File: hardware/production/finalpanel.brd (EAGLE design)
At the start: 166.7 x 33 mm, 49 parts, among them IC1 ATMEGA88

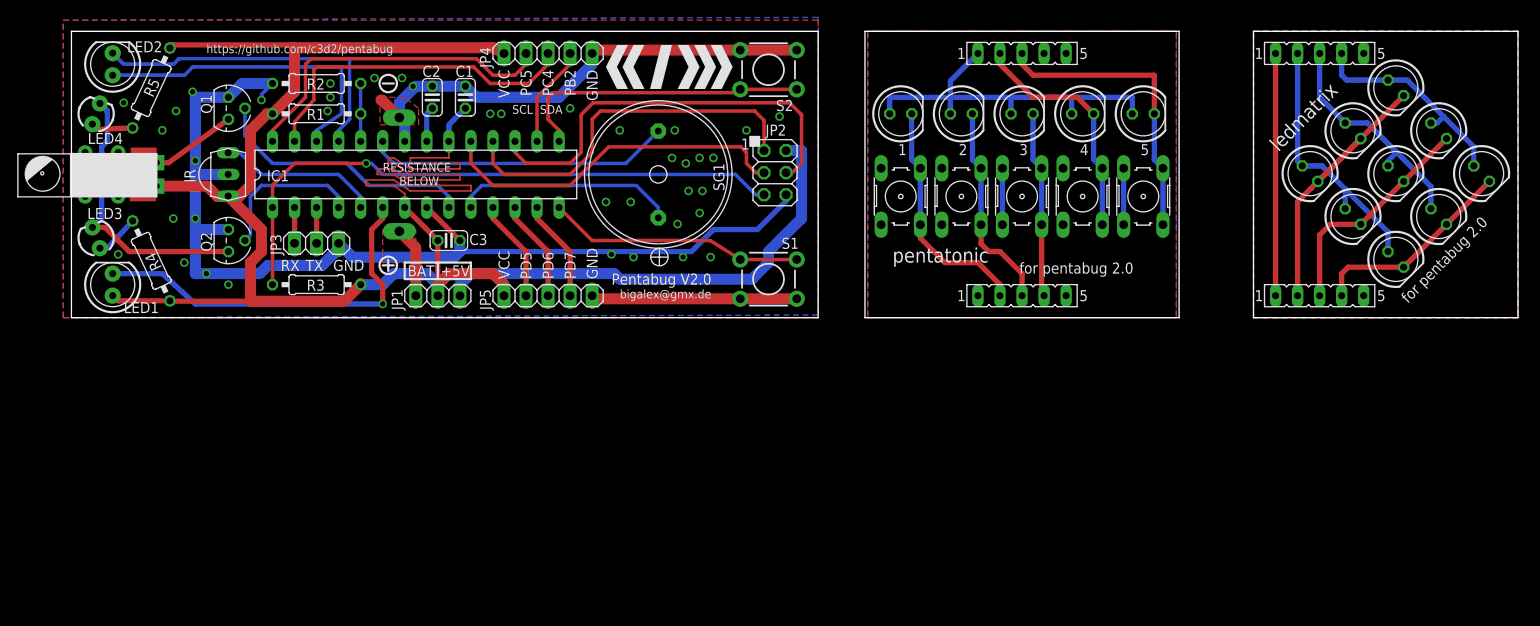
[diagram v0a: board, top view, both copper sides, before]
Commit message: correcting minor glitch (unrouted) in ledmatrix (thanks a lot to the guys from makepcb)
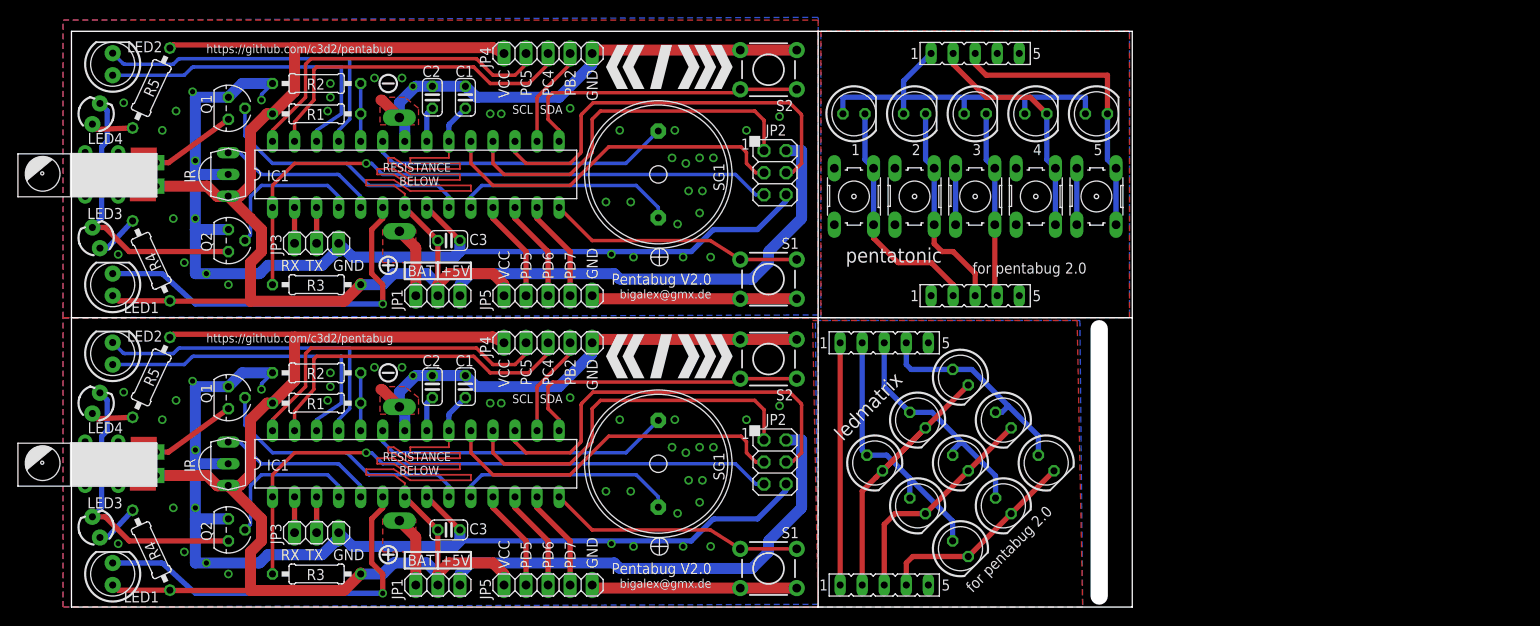
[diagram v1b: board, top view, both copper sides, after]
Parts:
- added BAT2: BATTERY_2XAAA, buglbr:BATTERY_2XAAA_SMALLPINS
- added C4, C5, C6: 100nF, resistor:C025-024X044
- added IC2: ATMEGA88, atmel:DIL28-3
- added IR1: TSOP382, buglbr:TSOP382
- added JP10, JP6: (no value), pinhead:1X03
- added JP7: (no value), pinhead:2X03
- added JP8, JP9: (no value), pinhead:1X05
- added LED19, LED20: (no value), SparkFun:LED5MM
- added LED21, LED22: (no value), SparkFun:LED3MM
- added Q3, Q4: (no value), transistors:TO-92
- added R10, R9: 22R, rcl:0207/10
- added R6: 10k, rcl:0207/10
- added R7: 100K, rcl:0207/10
- added R8: 22K, rcl:0207/10
- added S8, S9: (no value), SparkFun:TACTILE-PTH
- added SG2: MULTIBUZZRTDKBUZZR, buglbr:BUZZRTDK
- added U$2: VIBRAMOTOR, buglbr:LA4-432
- moved LED10 60.2 mm to (103.4, -6.86)
- moved LED11 60.2 mm to (108.3, -11.8)
- moved LED13 60.2 mm to (98.5, -11.8)
- moved LED14 60.2 mm to (103.4, -16.7)
- moved LED17 60.2 mm to (98.5, -21.7)
- moved LED18 60.2 mm to (103.4, -26.6)
- moved SV__4 60.2 mm to (94.6, -30.8)
- moved SV__5 60.2 mm to (94.6, -2.89)
- moved LED12 60.2 mm to (113.3, -16.7)
- moved LED15 60.2 mm to (108.3, -21.7)
- moved LED16 60.2 mm to (93.5, -16.7)
- moved LED5 5.40 mm to (91.1, 23.5)
- moved LED6 5.40 mm to (98.1, 23.5)
- moved LED7 5.40 mm to (105.1, 23.5)
- moved LED8 5.40 mm to (112.1, 23.5)
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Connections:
- new net +5V1: JP10.1, JP7.2
- new net BAT1: BAT2.+, JP10.3
- new net BATLVL1: IC2.24, R7.2, R8.1
- new net BUZGND1: IC2.23, SG2.-
- new net BUZZR1: IC2.10, SG2.+
- new net GND1: BAT2.-, C4.1, C5.1, C6.1, IC2.22, IC2.8, IR1.GND, JP6.3, JP7.6, JP8.5, JP9.5, Q3.1, Q4.1, R8.2, S8.3, S8.4, S9.3, S9.4
- new net IRREC1: IC2.5, IR1.OUT
- new net IRSEND1: IC2.4, Q4.2
- new net MISO1: IC2.18, JP7.1
- new net MOSI1: IC2.17, JP7.4
- new net N$13: Q3.3, U$2.P$2
- new net N$19: IC2.26, LED20.A
- new net N$20: IC2.25, LED20.K
- new net N$21: LED22.A, R10.1
- new net N$22: LED21.A, R9.1
- new net N$23: LED21.K, LED22.K, Q4.3
- new net N$24: IC2.6, LED19.K
- new net N$9: C5.2, IC2.21
- new net PB1: IC2.16, JP9.4
- new net PD1: IC2.11, JP8.2
- new net PD2: IC2.12, JP8.3
- new net PD3: IC2.13, JP8.4
- new net RST1: IC2.1, JP7.5, R6.1
- new net RX1: IC2.2, JP6.1
- new net S3: IC2.14, S9.1, S9.2
- new net S4: IC2.15, S8.1, S8.2
- new net SCK1: IC2.19, JP7.3
- new net SCL1: IC2.28, JP9.2
- new net SDA1: IC2.27, JP9.3
- new net TX1: IC2.3, JP6.2
- new net VCC1: C4.2, C6.2, IC2.20, IC2.7, IR1.VCC, JP10.2, JP8.1, JP9.1, LED19.A, R10.2, R6.2, R7.1, R9.2, U$2.P$1
- new net VIBRATE1: IC2.9, Q3.2
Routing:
- net VCC1: track 0.00 -> 225.7 mm
- net GND1: track 0.00 -> 201.9 mm, vias 0 -> 39
- net RST1: track 0.00 -> 70.6 mm, vias 0 -> 1
- net +5V1: track 0.00 -> 54.6 mm
- net MOSI1: track 0.00 -> 48.6 mm
- net N$24: track 0.00 -> 44.6 mm, vias 0 -> 1
- net MISO1: track 0.00 -> 43.5 mm
- net SCK1: track 0.00 -> 41.2 mm
- net SDA1: track 0.00 -> 39.2 mm
- net SCL1: track 0.00 -> 38.7 mm
- net N$20: track 0.00 -> 38.1 mm
- net N$19: track 0.00 -> 36.8 mm
- net BUZGND1: track 0.00 -> 35.1 mm
- net S4: track 0.00 -> 34.6 mm
- net N$23: track 0.00 -> 32.2 mm
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- added copper zone on layer 1, net BAT1
- added copper zone on layer 1, net GND1
- added copper zone on layer 16, net GND1
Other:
- board size 166.7 x 33 mm -> 122.2 x 66.3 mm
- board text added: "BAT1"
- board text added: "C1"
- board text added: "C2"
- board text added: "C3"
- board text added: "IC1"
- board text added: "JP1"
- board text added: "JP2"
- board text added: "JP3"
- board text added: "JP4"
- board text added: "JP5"
- board text added: "LED1"
- board text added: "LED2"
- board text added: "LED3"
- board text added: "LED4"
- board text added: "Q1"
- board text added: "Q2"
- board text added: "R1"
- board text added: "R2"
- board text added: "R3"
- board text added: "R4"
- board text added: "R5"
- board text added: "S1"
- board text added: "S2"
- board text added: "SG1"
